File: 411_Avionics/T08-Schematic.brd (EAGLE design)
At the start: 65.8 x 25.4 mm, 66 parts, among them IC1 BQ24022, J1 USB-MICROB, J3 JST-PH-2-SMT-RA, U1 LP5907, U2 M25P10-AVMN6TP_TR, U3 LSM9DS0, U5 LTC1998, U6 ATMEGA32U4-AU, X1 8MHz

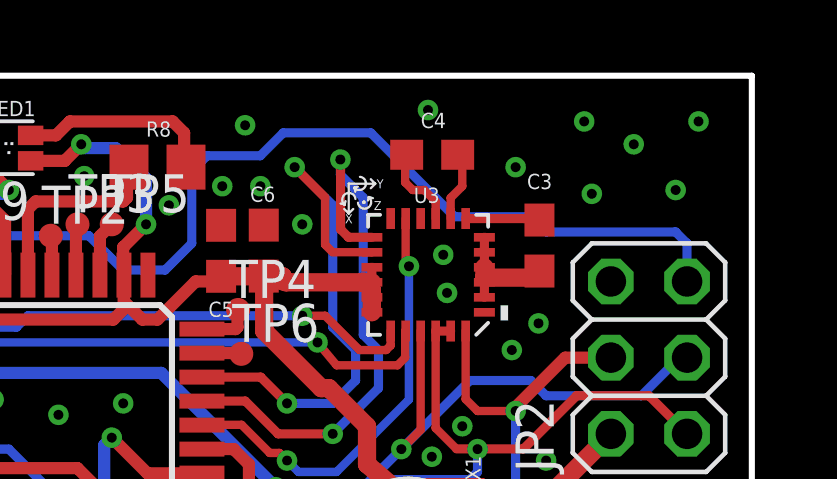
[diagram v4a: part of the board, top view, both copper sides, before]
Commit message: Added test points to accelerometer DRDY and DENB
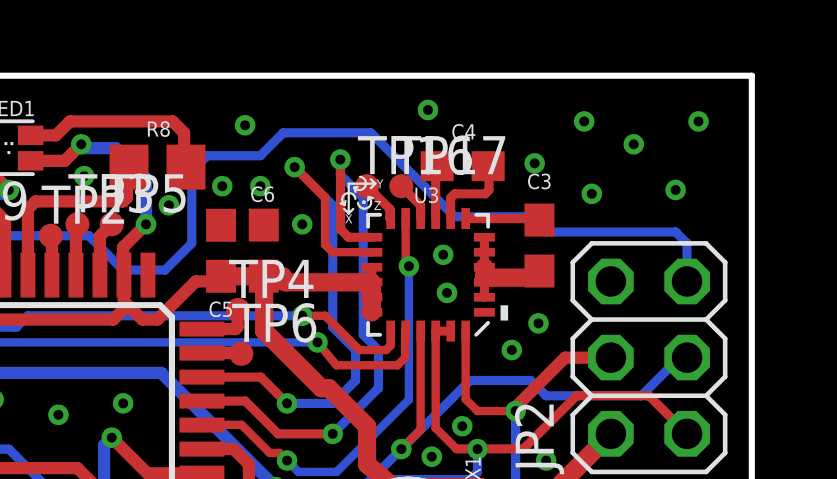
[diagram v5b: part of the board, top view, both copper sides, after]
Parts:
- added TP16, TP17: TPTP08R, testpad:TP08R
- moved C4 1.09 mm to (56.1, 22.4)
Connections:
- new net N$66: TP17.TP, U3.10
- new net N$67: TP16.TP, U3.12
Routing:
- net N$67: track 0.00 -> 1.42 mm
- net N$66: track 0.00 -> 1.34 mm
- net N$11: track 2.88 -> 1.77 mm
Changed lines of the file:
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@@
 <attribute name="NAME" x="59.128" y="22.13" size="0.508" layer="25" rot="R180"/>
 </element>
-<element name="C4" library="rcl" package="C0603" value=".22µ" x="55.131" y="22.766" smashed="yes">
-<attribute name="NAME" x="54.75" y="23.655" size="0.508" layer="25"/>
+<element name="C4" library="rcl" package="C0603" value=".22µ" x="56.147" y="22.385" smashed="yes">
+<attribute name="NAME" x="55.766" y="23.274" size="0.508" layer="25"/>
 </element>
 <element name="C5" library="rcl" package="C0603" value="2.2µ" x="48.094" y="19.564" smashed="yes" rot="R90">
@@
 </element>
 <element name="R17" library="rcl" package="R0603" value="0" x="35.687" y="18.923" rot="R90"/>
+<element name="TP16" library="testpad" package="TP08R" value="TPTP08R" x="52.959" y="21.717">
+<attribute name="TP_SIGNAL_NAME" value="" x="52.959" y="21.717" size="1.778" layer="27" display="off"/>
+</element>
+<element name="TP17" library="testpad" package="TP08R" value="TPTP08R" x="54.102" y="21.717">
+<attribute name="TP_SIGNAL_NAME" value="" x="54.102" y="21.717" size="1.778" layer="27" display="off"/>
+</element>
 </elements>
 <signals>
@@
 <via x="56.642" y="5.207" extent="1-16" drill="0.3302"/>
 <via x="56.515" y="1.27" extent="1-16" drill="0.3302"/>
-<via x="57.912" y="22.352" extent="1-16" drill="0.3302"/>
+<via x="58.547" y="22.479" extent="1-16" drill="0.3302"/>
 <via x="60.198" y="23.876" extent="1-16" drill="0.3302"/>
 <via x="60.452" y="21.463" extent="1-16" drill="0.3302"/>
@@
 <contactref element="C4" pad="2"/>
 <contactref element="U3" pad="8"/>
-<wire x1="56.083" y1="22.764" x2="55.981" y2="22.766" width="0.3048" layer="1"/>
-<wire x1="55.746" y1="20.639" x2="55.746" y2="21.329" width="0.2794" layer="1"/>
-<wire x1="55.746" y1="21.329" x2="56.134" y2="21.717" width="0.2794" layer="1"/>
-<wire x1="56.134" y1="21.717" x2="56.134" y2="22.713" width="0.2794" layer="1"/>
-<wire x1="56.134" y1="22.713" x2="55.981" y2="22.766" width="0.2794" layer="1"/>
+<wire x1="55.746" y1="20.639" x2="55.746" y2="21.329" width="0.3048" layer="1"/>
+<wire x1="55.746" y1="21.329" x2="55.88" y2="21.463" width="0.3048" layer="1"/>
+<wire x1="55.88" y1="21.463" x2="56.896" y2="21.463" width="0.3048" layer="1"/>
+<wire x1="56.896" y1="21.463" x2="57.023" y2="21.59" width="0.3048" layer="1"/>
+<wire x1="57.023" y1="21.59" x2="57.023" y2="22.359" width="0.3048" layer="1"/>
+<wire x1="57.023" y1="22.359" x2="56.997" y2="22.385" width="0.3048" layer="1"/>
 </signal>
 <signal name="N$11">
 <contactref element="C4" pad="1"/>
 <contactref element="U3" pad="9"/>
-<wire x1="54.198" y1="22.749" x2="54.281" y2="22.766" width="0.3048" layer="1"/>
-<wire x1="55.246" y1="20.639" x2="55.246" y2="21.208" width="0.2794" layer="1"/>
-<wire x1="55.246" y1="21.208" x2="54.864" y2="21.59" width="0.2794" layer="1"/>
-<wire x1="54.864" y1="21.59" x2="54.483" y2="21.59" width="0.2794" layer="1"/>
-<wire x1="54.483" y1="21.59" x2="54.229" y2="21.844" width="0.2794" layer="1"/>
-<wire x1="54.229" y1="21.844" x2="54.229" y2="22.718" width="0.2794" layer="1"/>
-<wire x1="54.229" y1="22.718" x2="54.281" y2="22.766" width="0.2794" layer="1"/>
+<wire x1="55.246" y1="20.639" x2="55.246" y2="22.334" width="0.3048" layer="1"/>
+<wire x1="55.246" y1="22.334" x2="55.297" y2="22.385" width="0.3048" layer="1"/>
 </signal>
 <signal name="VCC">
@@
 <wire x1="35.726" y1="19.812" x2="35.687" y2="19.773" width="0.4064" layer="1"/>
 </signal>
+<signal name="N$66">
+<contactref element="U3" pad="10"/>
+<contactref element="TP17" pad="TP"/>
+<wire x1="54.746" y1="20.639" x2="54.746" y2="21.073" width="0.3048" layer="1"/>
+<wire x1="54.746" y1="21.073" x2="54.102" y2="21.717" width="0.3048" layer="1"/>
+</signal>
+<signal name="N$67">
+<contactref element="TP16" pad="TP"/>
+<contactref element="U3" pad="12"/>
+<wire x1="53.746" y1="20.639" x2="53.721" y2="20.639" width="0.3048" layer="1"/>
+<wire x1="53.721" y1="20.639" x2="53.721" y2="20.955" width="0.3048" layer="1"/>
+<wire x1="53.721" y1="20.955" x2="52.959" y2="21.717" width="0.3048" layer="1"/>
+</signal>
 </signals>
